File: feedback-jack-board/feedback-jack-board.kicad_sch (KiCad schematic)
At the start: 6 parts, among them J1 Out, J2 Ret, J3 In, J4 Snd, J5 908140508, J6 Barrel_Jack_Switch

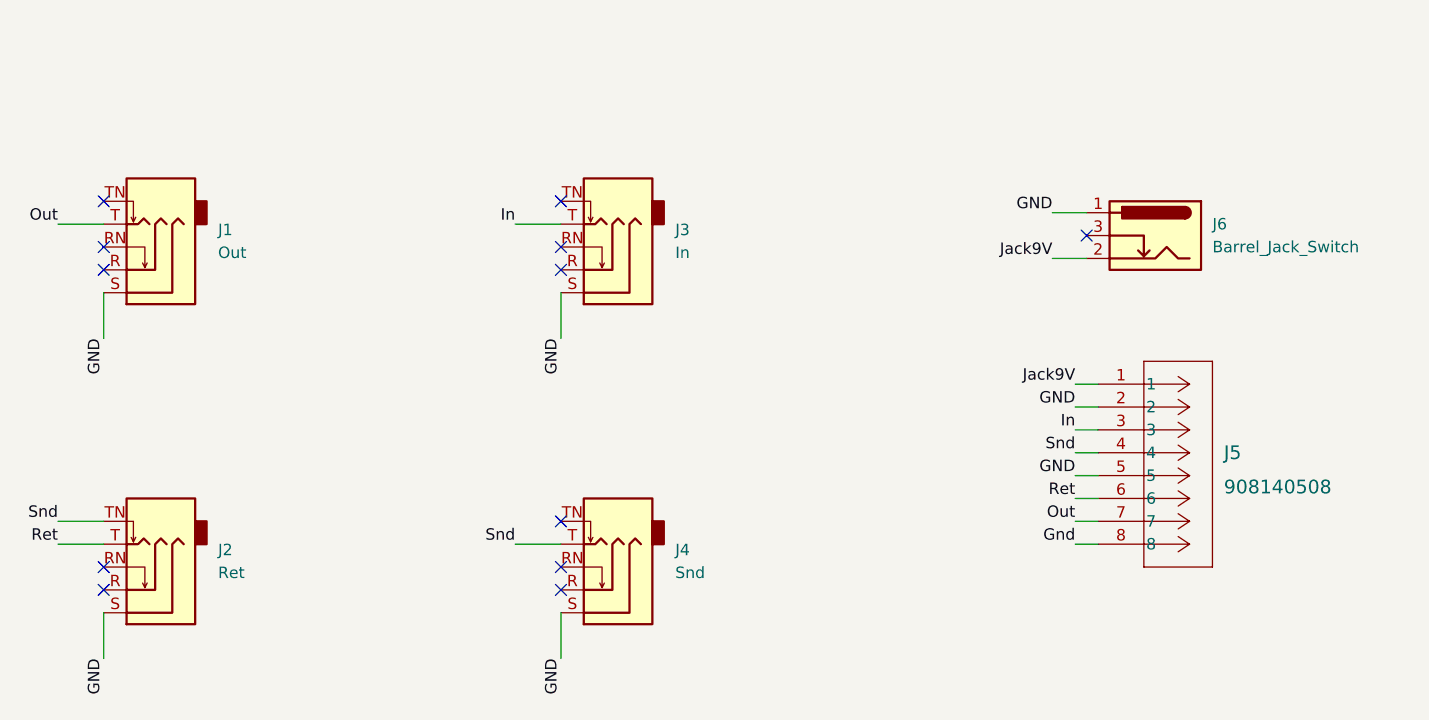
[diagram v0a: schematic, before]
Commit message: JFET switching + reroute + FBD connector
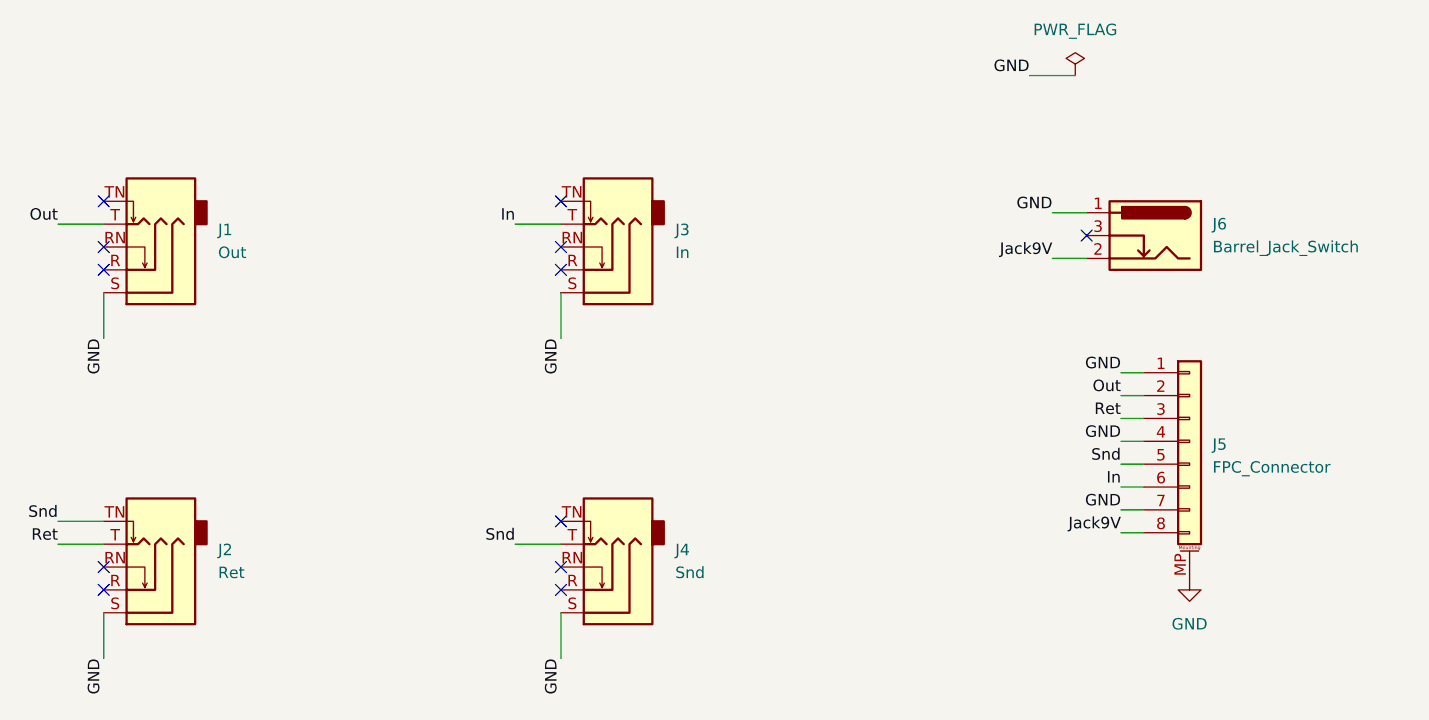
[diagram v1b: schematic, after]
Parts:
- removed J5: 908140508, molex-picoflex8:CONN_SDA-90814_08_MOL, symbol molex-picoflex8:908140508
- added J5: FPC_Connector, Connector_FFC-FPC:JUSHUO_AFA07-S08FCA-00_1x8-1MP_P1.0mm_Horizontal, symbol Connector_Generic_MountingPin:Conn_01x08_MountingPin
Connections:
- net GND: now also J5.1 (Pin_1), J5.4 (Pin_4), J5.7 (Pin_7), J5.MP (MountPin)
- net In: now also J5.6 (Pin_6)
- net Jack9V: now also J5.8 (Pin_8)
- net Out: now also J5.2 (Pin_2)
- net Ret: now also J5.3 (Pin_3)
- net Snd: now also J5.5 (Pin_5)
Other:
- company: Pedal Markt / Andrei Salomatin -> Andrei Salomatin / akkusativ
